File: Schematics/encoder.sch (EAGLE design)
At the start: 2 parts, among them U1 ENCODER_2LED

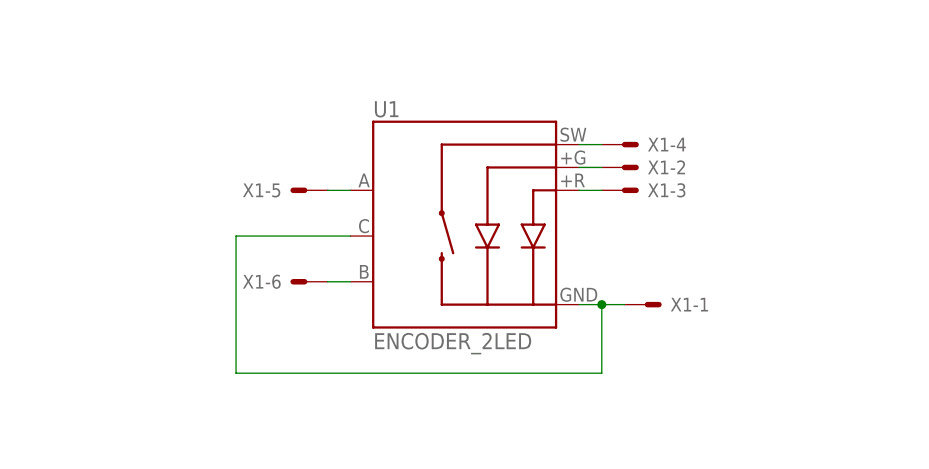
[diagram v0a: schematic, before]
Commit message: Add caps to encoder breakout
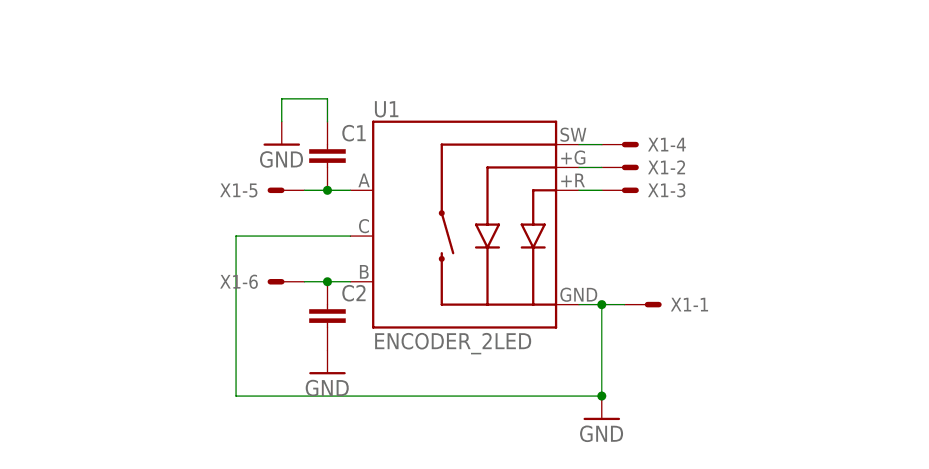
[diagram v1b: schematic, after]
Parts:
- added C1, C2: (no value), rcl:C-EU025-024X044
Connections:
- removed net N$1: U1.-, U1.C, X1-1.S
- new net GND: C1.1, C2.2, U1.-, U1.C, X1-1.S
- net N$5: now also C1.2
- net N$6: now also C2.1
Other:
- moved on the sheet: X1-5, X1-6
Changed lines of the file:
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@@
 <part name="U1" library="SparkFun" deviceset="ENCODER_2LED" device=""/>
 <part name="X1" library="con-molex" deviceset="22-23-2061" device=""/>
+<part name="C1" library="rcl" deviceset="C-EU" device="025-024X044"/>
+<part name="C2" library="rcl" deviceset="C-EU" device="025-024X044"/>
+<part name="GND1" library="supply1" deviceset="GND" device=""/>
+<part name="GND2" library="supply1" deviceset="GND" device=""/>
+<part name="GND3" library="supply1" deviceset="GND" device=""/>
 </parts>
 <sheets>
@@
 <instance part="X1" gate="-3" x="43.18" y="35.56"/>
 <instance part="X1" gate="-4" x="43.18" y="40.64"/>
-<instance part="X1" gate="-5" x="7.62" y="35.56" rot="R180"/>
-<instance part="X1" gate="-6" x="7.62" y="25.4" rot="R180"/>
+<instance part="X1" gate="-5" x="5.08" y="35.56" rot="R180"/>
+<instance part="X1" gate="-6" x="5.08" y="25.4" rot="R180"/>
+<instance part="C1" gate="G$1" x="10.16" y="40.64"/>
+<instance part="C2" gate="G$1" x="10.16" y="22.86"/>
+<instance part="GND1" gate="1" x="10.16" y="15.24"/>
+<instance part="GND2" gate="1" x="5.08" y="40.64"/>
+<instance part="GND3" gate="1" x="40.64" y="10.16"/>
 </instances>
 <busses>
@@
 <pinref part="U1" gate="G$1" pin="A"/>
 <pinref part="X1" gate="-5" pin="S"/>
+<wire x1="7.62" y1="35.56" x2="10.16" y2="35.56" width="0.1524" layer="91"/>
+<pinref part="C1" gate="G$1" pin="2"/>
 <wire x1="10.16" y1="35.56" x2="12.7" y2="35.56" width="0.1524" layer="91"/>
+<junction x="10.16" y="35.56"/>
 </segment>
 </net>
@@
 <pinref part="U1" gate="G$1" pin="B"/>
 <pinref part="X1" gate="-6" pin="S"/>
+<wire x1="7.62" y1="25.4" x2="10.16" y2="25.4" width="0.1524" layer="91"/>
+<pinref part="C2" gate="G$1" pin="1"/>
 <wire x1="10.16" y1="25.4" x2="12.7" y2="25.4" width="0.1524" layer="91"/>
+<junction x="10.16" y="25.4"/>
 </segment>
 </net>
-<net name="N$1" class="0">
+<net name="GND" class="0">
+<segment>
+<pinref part="C2" gate="G$1" pin="2"/>
+<pinref part="GND1" gate="1" pin="GND"/>
+</segment>
 <segment>
 <pinref part="U1" gate="G$1" pin="C"/>
 <wire x1="12.7" y1="30.48" x2="0" y2="30.48" width="0.1524" layer="91"/>
-<wire x1="0" y1="30.48" x2="0" y2="15.24" width="0.1524" layer="91"/>
-<wire x1="0" y1="15.24" x2="40.64" y2="15.24" width="0.1524" layer="91"/>
+<wire x1="0" y1="30.48" x2="0" y2="12.7" width="0.1524" layer="91"/>
+<wire x1="0" y1="12.7" x2="40.64" y2="12.7" width="0.1524" layer="91"/>
 <pinref part="U1" gate="G$1" pin="-"/>
 <wire x1="38.1" y1="22.86" x2="40.64" y2="22.86" width="0.1524" layer="91"/>
 <pinref part="X1" gate="-1" pin="S"/>
 <wire x1="40.64" y1="22.86" x2="43.18" y2="22.86" width="0.1524" layer="91"/>
-<wire x1="40.64" y1="15.24" x2="40.64" y2="22.86" width="0.1524" layer="91"/>
+<wire x1="40.64" y1="12.7" x2="40.64" y2="22.86" width="0.1524" layer="91"/>
 <junction x="40.64" y="22.86"/>
+<pinref part="GND3" gate="1" pin="GND"/>
+<junction x="40.64" y="12.7"/>
+</segment>
+<segment>
+<pinref part="C1" gate="G$1" pin="1"/>
+<wire x1="10.16" y1="43.18" x2="10.16" y2="45.72" width="0.1524" layer="91"/>
+<pinref part="GND2" gate="1" pin="GND"/>
+<wire x1="10.16" y1="45.72" x2="5.08" y2="45.72" width="0.1524" layer="91"/>
+<wire x1="5.08" y1="45.72" x2="5.08" y2="43.18" width="0.1524" layer="91"/>
 </segment>
 </net>

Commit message: Add current limiting resistors for LEDs
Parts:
- added R1, R2: (no value), rcl:R-EU_R0603
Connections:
- new net N$1: R1.2, X1-2.S
- new net N$7: R2.1, U1.+R
- net N$2: now also R2.2, X1-3.S; no longer U1.+G, X1-2.S
- net N$3: now also R1.1, U1.+G; no longer U1.+R, X1-3.S
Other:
- moved on the sheet: X1-2, X1-3, X1-4
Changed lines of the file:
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@@
 <part name="GND2" library="supply1" deviceset="GND" device=""/>
 <part name="GND3" library="supply1" deviceset="GND" device=""/>
+<part name="R1" library="rcl" deviceset="R-EU_" device="R0603"/>
+<part name="R2" library="rcl" deviceset="R-EU_" device="R0603"/>
 </parts>
 <sheets>
@@
 <instance part="U1" gate="G$1" x="25.4" y="30.48"/>
 <instance part="X1" gate="-1" x="45.72" y="22.86"/>
-<instance part="X1" gate="-2" x="43.18" y="38.1"/>
-<instance part="X1" gate="-3" x="43.18" y="35.56"/>
-<instance part="X1" gate="-4" x="43.18" y="40.64"/>
+<instance part="X1" gate="-2" x="66.04" y="38.1"/>
+<instance part="X1" gate="-3" x="66.04" y="35.56"/>
+<instance part="X1" gate="-4" x="40.64" y="45.72" rot="R90"/>
 <instance part="X1" gate="-5" x="5.08" y="35.56" rot="R180"/>
 <instance part="X1" gate="-6" x="5.08" y="25.4" rot="R180"/>
@@
 <instance part="GND2" gate="1" x="5.08" y="40.64"/>
 <instance part="GND3" gate="1" x="40.64" y="10.16"/>
+<instance part="R1" gate="G$1" x="45.72" y="38.1"/>
+<instance part="R2" gate="G$1" x="55.88" y="35.56"/>
 </instances>
 <busses>
 </busses>
 <nets>
-<net name="N$2" class="0">
-<segment>
-<pinref part="U1" gate="G$1" pin="+G"/>
-<pinref part="X1" gate="-2" pin="S"/>
-<wire x1="40.64" y1="38.1" x2="38.1" y2="38.1" width="0.1524" layer="91"/>
-</segment>
-</net>
-<net name="N$3" class="0">
-<segment>
-<pinref part="U1" gate="G$1" pin="+R"/>
-<pinref part="X1" gate="-3" pin="S"/>
-<wire x1="40.64" y1="35.56" x2="38.1" y2="35.56" width="0.1524" layer="91"/>
-</segment>
-</net>
 <net name="N$4" class="0">
 <segment>
 <pinref part="U1" gate="G$1" pin="SW"/>
 <pinref part="X1" gate="-4" pin="S"/>
+<wire x1="40.64" y1="43.18" x2="40.64" y2="40.64" width="0.1524" layer="91"/>
 <wire x1="40.64" y1="40.64" x2="38.1" y2="40.64" width="0.1524" layer="91"/>
 </segment>
@@
 </segment>
 </net>
+<net name="N$1" class="0">
+<segment>
+<pinref part="X1" gate="-2" pin="S"/>
+<pinref part="R1" gate="G$1" pin="2"/>
+<wire x1="63.5" y1="38.1" x2="50.8" y2="38.1" width="0.1524" layer="91"/>
+</segment>
+</net>
+<net name="N$2" class="0">
+<segment>
+<pinref part="X1" gate="-3" pin="S"/>
+<pinref part="R2" gate="G$1" pin="2"/>
+<wire x1="63.5" y1="35.56" x2="60.96" y2="35.56" width="0.1524" layer="91"/>
+</segment>
+</net>
+<net name="N$3" class="0">
+<segment>
+<pinref part="U1" gate="G$1" pin="+G"/>
+<pinref part="R1" gate="G$1" pin="1"/>
+<wire x1="38.1" y1="38.1" x2="40.64" y2="38.1" width="0.1524" layer="91"/>
+</segment>
+</net>
+<net name="N$7" class="0">
+<segment>
+<pinref part="R2" gate="G$1" pin="1"/>
+<pinref part="U1" gate="G$1" pin="+R"/>
+<wire x1="50.8" y1="35.56" x2="38.1" y2="35.56" width="0.1524" layer="91"/>
+</segment>
+</net>

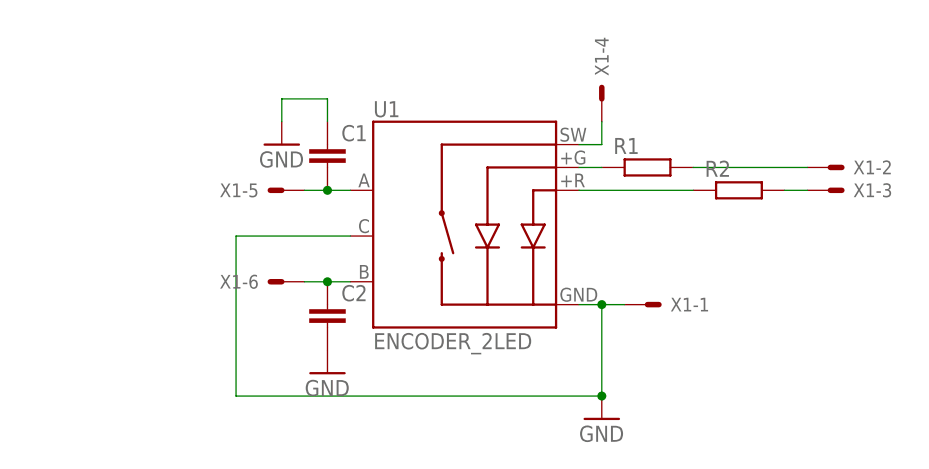
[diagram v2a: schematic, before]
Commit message: bromotimer PCB: added low pass filter to encoder
Added LPF to avoid chattering, added holes to encoder pcb.
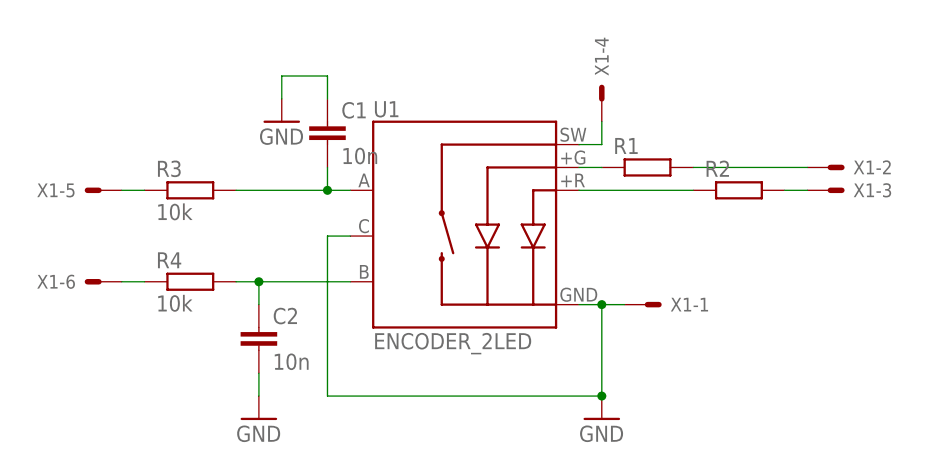
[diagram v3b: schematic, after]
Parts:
- added R3, R4: 10k, rcl:R-EU_R0603
- C1, C2: value (none) -> 10n
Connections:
- new net N$8: R4.1, X1-6.S
- new net N$9: R3.1, X1-5.S
- net N$5: now also R3.2; no longer X1-5.S
- net N$6: now also R4.2; no longer X1-6.S
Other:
- moved on the sheet: C1, C2, X1-5, X1-6
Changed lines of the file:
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@@
 <part name="U1" library="SparkFun" deviceset="ENCODER_2LED" device=""/>
 <part name="X1" library="con-molex" deviceset="22-23-2061" device=""/>
-<part name="C1" library="rcl" deviceset="C-EU" device="025-024X044"/>
-<part name="C2" library="rcl" deviceset="C-EU" device="025-024X044"/>
+<part name="C1" library="rcl" deviceset="C-EU" device="025-024X044" value="10n"/>
+<part name="C2" library="rcl" deviceset="C-EU" device="025-024X044" value="10n"/>
 <part name="GND1" library="supply1" deviceset="GND" device=""/>
 <part name="GND2" library="supply1" deviceset="GND" device=""/>
@@
 <part name="R1" library="rcl" deviceset="R-EU_" device="R0603"/>
 <part name="R2" library="rcl" deviceset="R-EU_" device="R0603"/>
+<part name="R3" library="rcl" deviceset="R-EU_" device="R0603" value="10k"/>
+<part name="R4" library="rcl" deviceset="R-EU_" device="R0603" value="10k"/>
 </parts>
 <sheets>
@@
 <instance part="X1" gate="-3" x="66.04" y="35.56"/>
 <instance part="X1" gate="-4" x="40.64" y="45.72" rot="R90"/>
-<instance part="X1" gate="-5" x="5.08" y="35.56" rot="R180"/>
-<instance part="X1" gate="-6" x="5.08" y="25.4" rot="R180"/>
-<instance part="C1" gate="G$1" x="10.16" y="40.64"/>
-<instance part="C2" gate="G$1" x="10.16" y="22.86"/>
-<instance part="GND1" gate="1" x="10.16" y="15.24"/>
-<instance part="GND2" gate="1" x="5.08" y="40.64"/>
+<instance part="X1" gate="-5" x="-15.24" y="35.56" rot="R180"/>
+<instance part="X1" gate="-6" x="-15.24" y="25.4" rot="R180"/>
+<instance part="C1" gate="G$1" x="10.16" y="43.18"/>
+<instance part="C2" gate="G$1" x="2.54" y="20.32"/>
+<instance part="GND1" gate="1" x="2.54" y="10.16"/>
+<instance part="GND2" gate="1" x="5.08" y="43.18"/>
 <instance part="GND3" gate="1" x="40.64" y="10.16"/>
 <instance part="R1" gate="G$1" x="45.72" y="38.1"/>
 <instance part="R2" gate="G$1" x="55.88" y="35.56"/>
+<instance part="R3" gate="G$1" x="-5.08" y="35.56"/>
+<instance part="R4" gate="G$1" x="-5.08" y="25.4"/>
 </instances>
 <busses>
@@
 <segment>
 <pinref part="U1" gate="G$1" pin="A"/>
-<pinref part="X1" gate="-5" pin="S"/>
-<wire x1="7.62" y1="35.56" x2="10.16" y2="35.56" width="0.1524" layer="91"/>
 <pinref part="C1" gate="G$1" pin="2"/>
+<wire x1="10.16" y1="38.1" x2="10.16" y2="35.56" width="0.1524" layer="91"/>
 <wire x1="10.16" y1="35.56" x2="12.7" y2="35.56" width="0.1524" layer="91"/>
+<pinref part="R3" gate="G$1" pin="2"/>
+<wire x1="0" y1="35.56" x2="10.16" y2="35.56" width="0.1524" layer="91"/>
 <junction x="10.16" y="35.56"/>
 </segment>
@@
 <segment>
 <pinref part="U1" gate="G$1" pin="B"/>
-<pinref part="X1" gate="-6" pin="S"/>
-<wire x1="7.62" y1="25.4" x2="10.16" y2="25.4" width="0.1524" layer="91"/>
 <pinref part="C2" gate="G$1" pin="1"/>
-<wire x1="10.16" y1="25.4" x2="12.7" y2="25.4" width="0.1524" layer="91"/>
-<junction x="10.16" y="25.4"/>
+<wire x1="2.54" y1="22.86" x2="2.54" y2="25.4" width="0.1524" layer="91"/>
+<wire x1="2.54" y1="25.4" x2="12.7" y2="25.4" width="0.1524" layer="91"/>
+<pinref part="R4" gate="G$1" pin="2"/>
+<wire x1="0" y1="25.4" x2="2.54" y2="25.4" width="0.1524" layer="91"/>
+<junction x="2.54" y="25.4"/>
 </segment>
 </net>
@@
 <pinref part="C2" gate="G$1" pin="2"/>
 <pinref part="GND1" gate="1" pin="GND"/>
+<wire x1="2.54" y1="15.24" x2="2.54" y2="12.7" width="0.1524" layer="91"/>
 </segment>
 <segment>
 <pinref part="U1" gate="G$1" pin="C"/>
-<wire x1="12.7" y1="30.48" x2="0" y2="30.48" width="0.1524" layer="91"/>
-<wire x1="0" y1="30.48" x2="0" y2="12.7" width="0.1524" layer="91"/>
-<wire x1="0" y1="12.7" x2="40.64" y2="12.7" width="0.1524" layer="91"/>
+<wire x1="12.7" y1="30.48" x2="10.16" y2="30.48" width="0.1524" layer="91"/>
+<wire x1="10.16" y1="30.48" x2="10.16" y2="12.7" width="0.1524" layer="91"/>
+<wire x1="10.16" y1="12.7" x2="40.64" y2="12.7" width="0.1524" layer="91"/>
 <pinref part="U1" gate="G$1" pin="-"/>
 <wire x1="38.1" y1="22.86" x2="40.64" y2="22.86" width="0.1524" layer="91"/>
@@
 <segment>
 <pinref part="C1" gate="G$1" pin="1"/>
-<wire x1="10.16" y1="43.18" x2="10.16" y2="45.72" width="0.1524" layer="91"/>
+<wire x1="10.16" y1="45.72" x2="10.16" y2="48.26" width="0.1524" layer="91"/>
 <pinref part="GND2" gate="1" pin="GND"/>
-<wire x1="10.16" y1="45.72" x2="5.08" y2="45.72" width="0.1524" layer="91"/>
-<wire x1="5.08" y1="45.72" x2="5.08" y2="43.18" width="0.1524" layer="91"/>
+<wire x1="10.16" y1="48.26" x2="5.08" y2="48.26" width="0.1524" layer="91"/>
+<wire x1="5.08" y1="48.26" x2="5.08" y2="45.72" width="0.1524" layer="91"/>
 </segment>
 </net>
@@
 </segment>
 </net>
+<net name="N$8" class="0">
+<segment>
+<pinref part="X1" gate="-6" pin="S"/>
+<pinref part="R4" gate="G$1" pin="1"/>
+<wire x1="-12.7" y1="25.4" x2="-10.16" y2="25.4" width="0.1524" layer="91"/>
+</segment>
+</net>
+<net name="N$9" class="0">
+<segment>
+<pinref part="X1" gate="-5" pin="S"/>
+<pinref part="R3" gate="G$1" pin="1"/>
+<wire x1="-12.7" y1="35.56" x2="-10.16" y2="35.56" width="0.1524" layer="91"/>
+</segment>
+</net>
